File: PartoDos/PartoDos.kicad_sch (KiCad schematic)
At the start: 58 parts, among them J1 RED4, J10 WHI4, J11 RED5, J12 GRE3, J13 GNC_BOND, J14 GNC_BOND, J15 GNC_BOND, J16 GNC_BOND, J17 GNC_BOND, J18 GNC_BOND, J19 GNC_BOND, J2 YEL4, J20 GNC_BOND, J21 GNC_BOND, J22 GNC_BOND, J23 GNC_BOND, J24 GNC_BOND, J25 GNC_BOND, J26 GNC_BOND, J27 GNC_BOND, J28 GNC_BOND, J29 GNC_BOND, J3 BLU1, J30 GNC_BOND, J31 GNC_BOND, J32 GNC_BOND, J33 GNC_BOND, J34 GNC_BOND, J4 YEL3, J5 GRE1, J6 WHI3, J7 GRE2, J8 BLU2, J9 YEL5

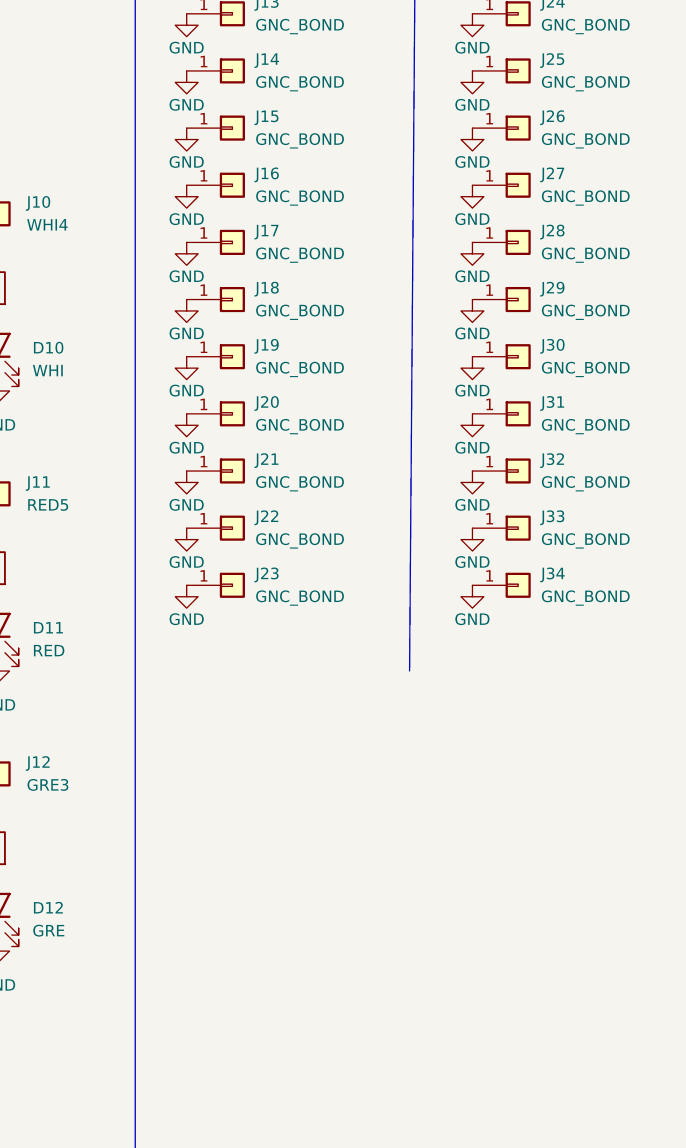
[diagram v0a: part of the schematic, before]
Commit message: Fixed code
Had an issue in shiftOutData where I defined the wrong data type (16 bit instead of 32 bit) so it cut all data short
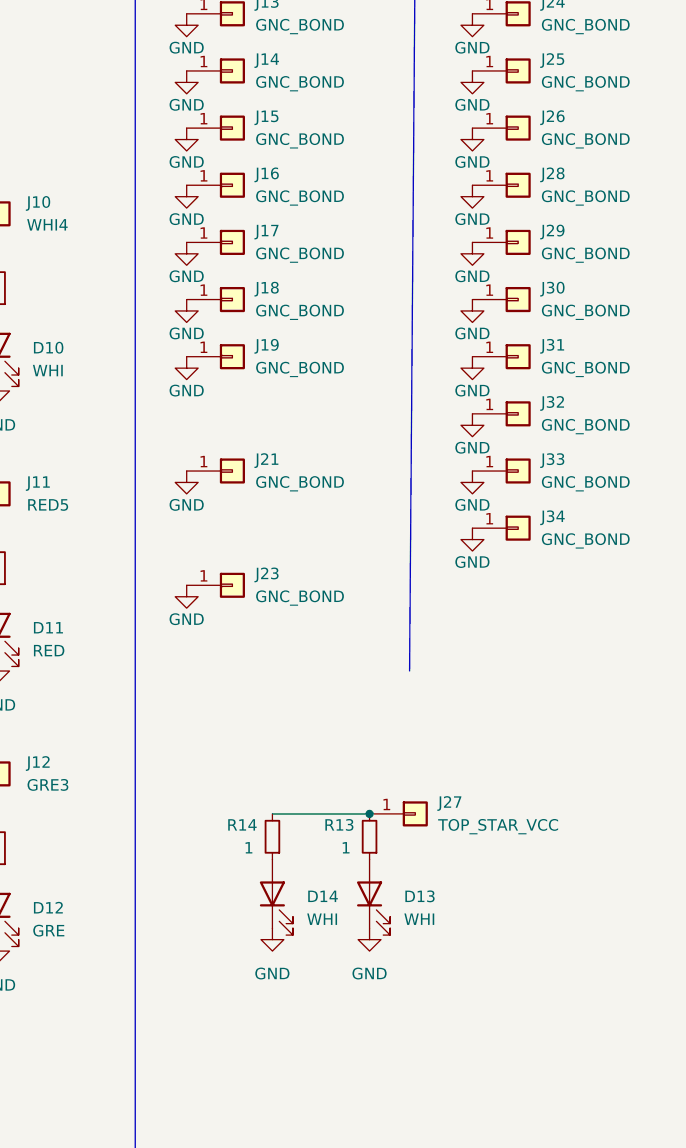
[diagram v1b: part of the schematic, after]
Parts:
- removed J20, J22: GNC_BOND, Connector_Wire:SolderWirePad_1x01_SMD_1x2mm, symbol Connector_Generic:Conn_01x01
- added D13, D14: WHI, LED_SMD:LED_0805_2012Metric, symbol Device:LED
- added R13, R14: 1, Resistor_SMD:R_1206_3216Metric, symbol Device:R_Small
- J27: value GNC_BOND -> TOP_STAR_VCC
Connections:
- net GND: now also D13.1 (K), D14.1 (K); no longer J27.1 (Pin_1)
- new net: D13.2 (A), R13.1
- new net: J27.1 (Pin_1), R13.2, R14.2
- new net: D14.2 (A), R14.1
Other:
- moved on the sheet: J27, J28, J29, J30, J31, J32, J33, J34

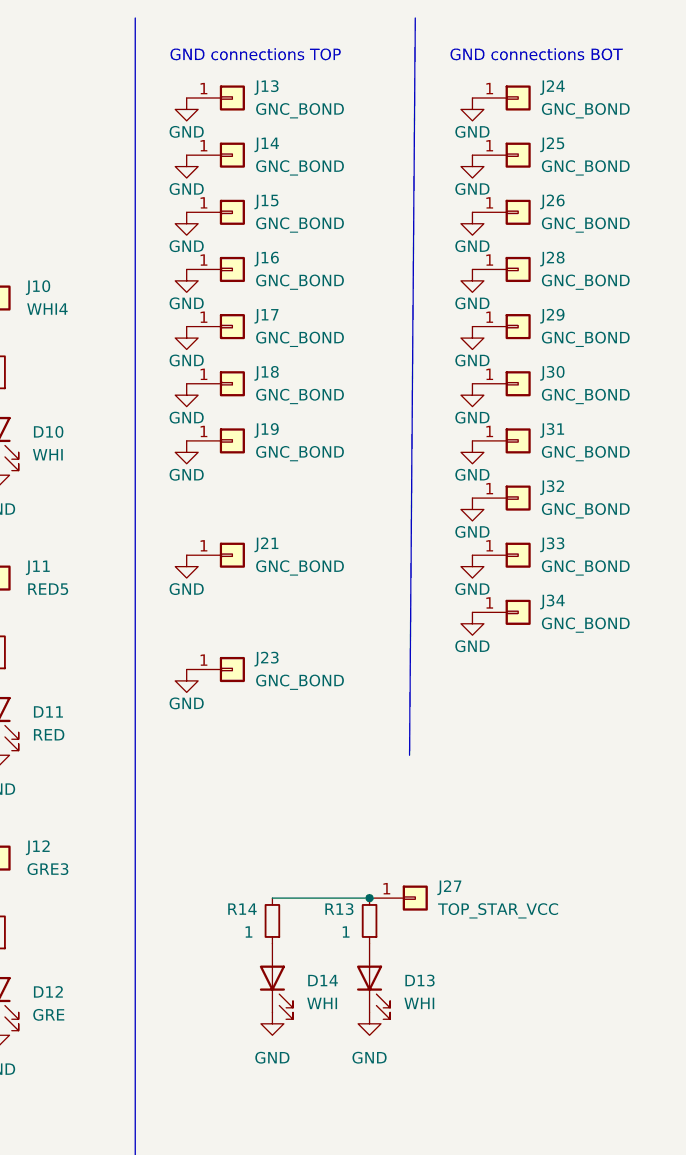
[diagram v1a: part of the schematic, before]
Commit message: Updated design
+ top LED
+ power switch
~ routing
~ via stitching more aligned
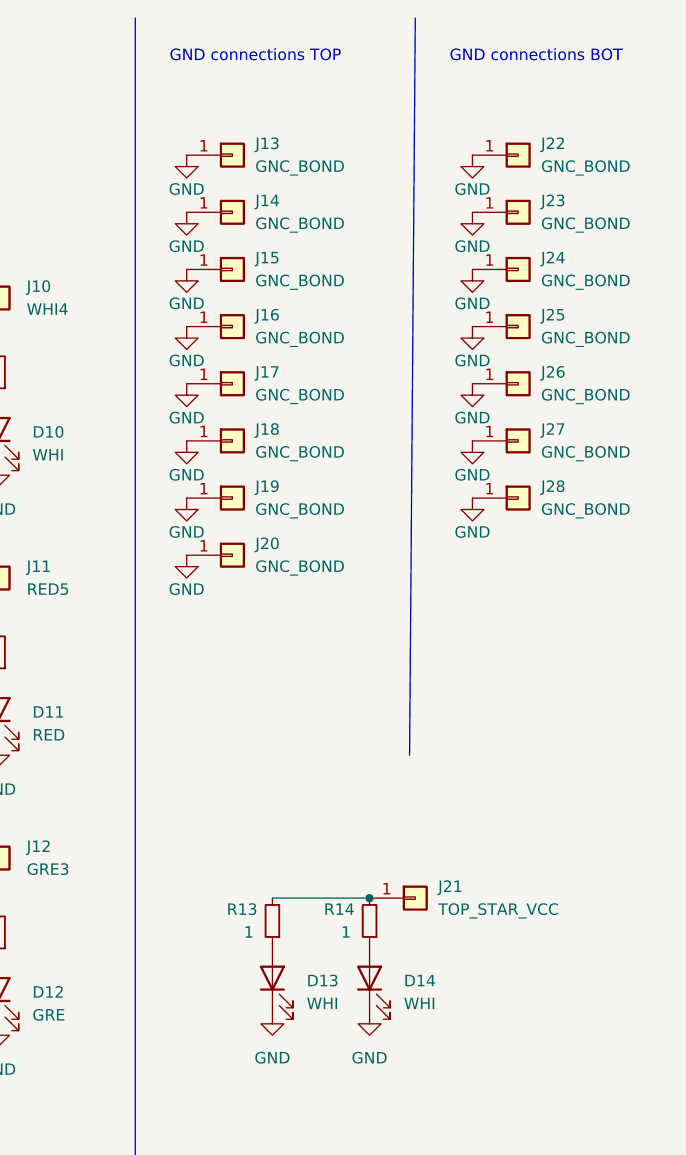
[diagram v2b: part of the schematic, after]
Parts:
- removed J13, J29, J31, J33: GNC_BOND, Connector_Wire:SolderWirePad_1x01_SMD_1x2mm, symbol Connector_Generic:Conn_01x01
- renumbered D14 to D13, D13 to D14, J14 to J13, J15 to J14, J16 to J15, J17 to J16, J18 to J17, J19 to J18, J21 to J19, J23 to J20, J27 to J21, J24 to J22, J25 to J23, J26 to J24, J28 to J25, J30 to J26, J32 to J27, J34 to J28, R14 to R13, R13 to R14
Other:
- moved on the sheet: J19, J20, J22, J23, J24, J25, J27, J28
